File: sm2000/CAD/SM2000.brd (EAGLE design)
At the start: 160 x 100 mm, 344 parts, among them CN1 HDR100-3, CN10 ST-3509, CN11 HDR100-3, CN2 JS-MU3-002, CN3 DS-0518, CN5 ST-3509, CN8 ST-3509, J1 JMP-2PIN, J2 JMP-2PIN, J3 JMP-2PIN, J4 CONN-BOOM-XH-2A, P10 TPAD50, P11 TPAD50, P12 TPAD50, P13 TPAD50, P14 TPAD50, P16 TPAD50, P18 TPAD50, P19 TPAD50, P20 TPAD50, P21 TPAD50, P3 TPAD50, P4 TPAD50, P5 TPAD50, P6 TPAD50, P7 TPAD50, P8 TPAD50, P9 TPAD50, Q1 MMBT3904, Q12 BRF92, Q13 BFQ19, Q14 RD01MUS2, Q17 MMT2904, Q18 MMT2904, Q2 MMBT3904, Q3 MMBT3904, Q4 MMBT3904, Q5 MMBT3904, Q6 MMBT3904, Q7 BC548, Q8 BC549, SW1 SW-LC2259, SW2 TS-026, SW3 SW-LC2259EENP, SW4 TS-026, SW5 TS-02B, U1 STM32F405VGT6, U10 DNL, U12 PGA-103+, U13 ADE-1, U2 LD3985M33R, U3 STMPS2141, U4 EMIF02-USB03F2, U5 TPS54329E, U7 SA612A, U8 LM386M-1, U9 LMV341, X1 BU-SMA-H, X2 BU-SMA-H

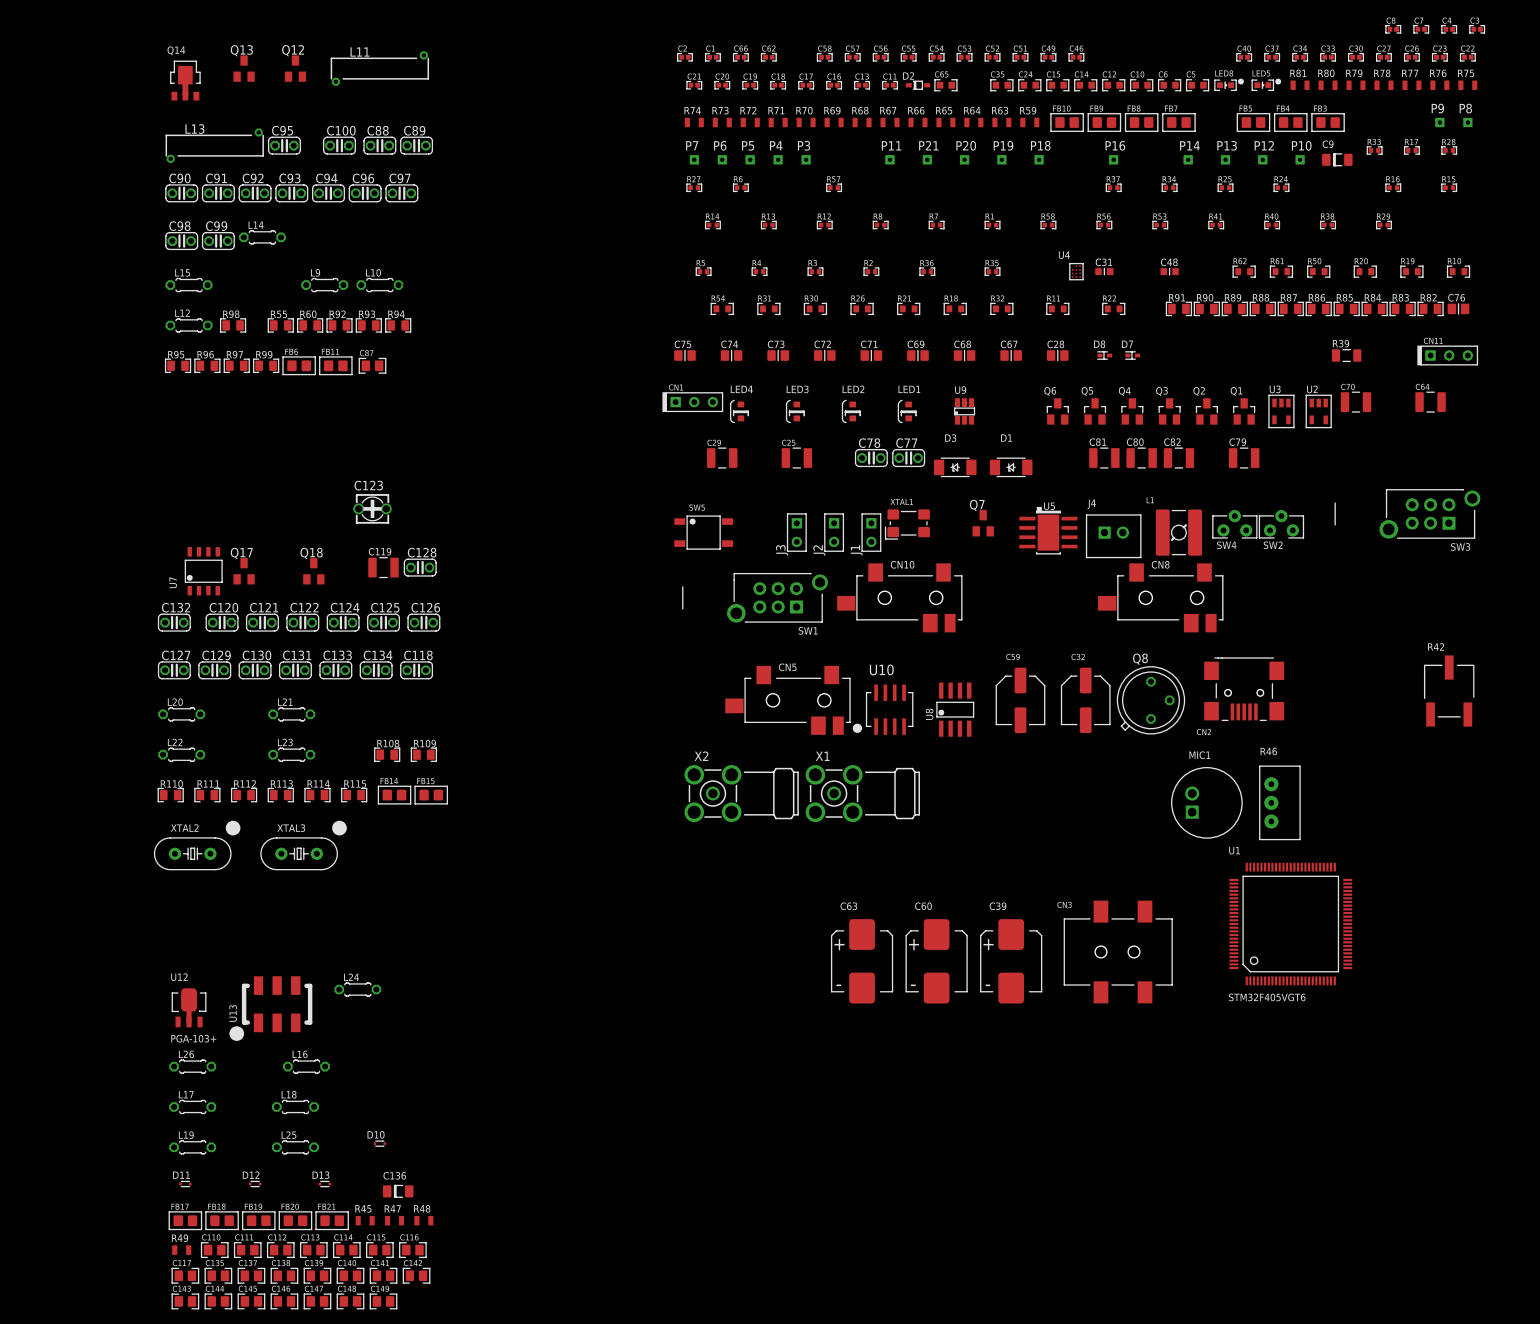
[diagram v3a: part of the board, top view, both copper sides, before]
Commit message: aDDED lOCAL oSCILLATOR CIRCUITRY TO sm2000 sch. MOVED 3.3V PS TO SHT 4. CONTINUED SCHEMATIC CLEANUP RGB
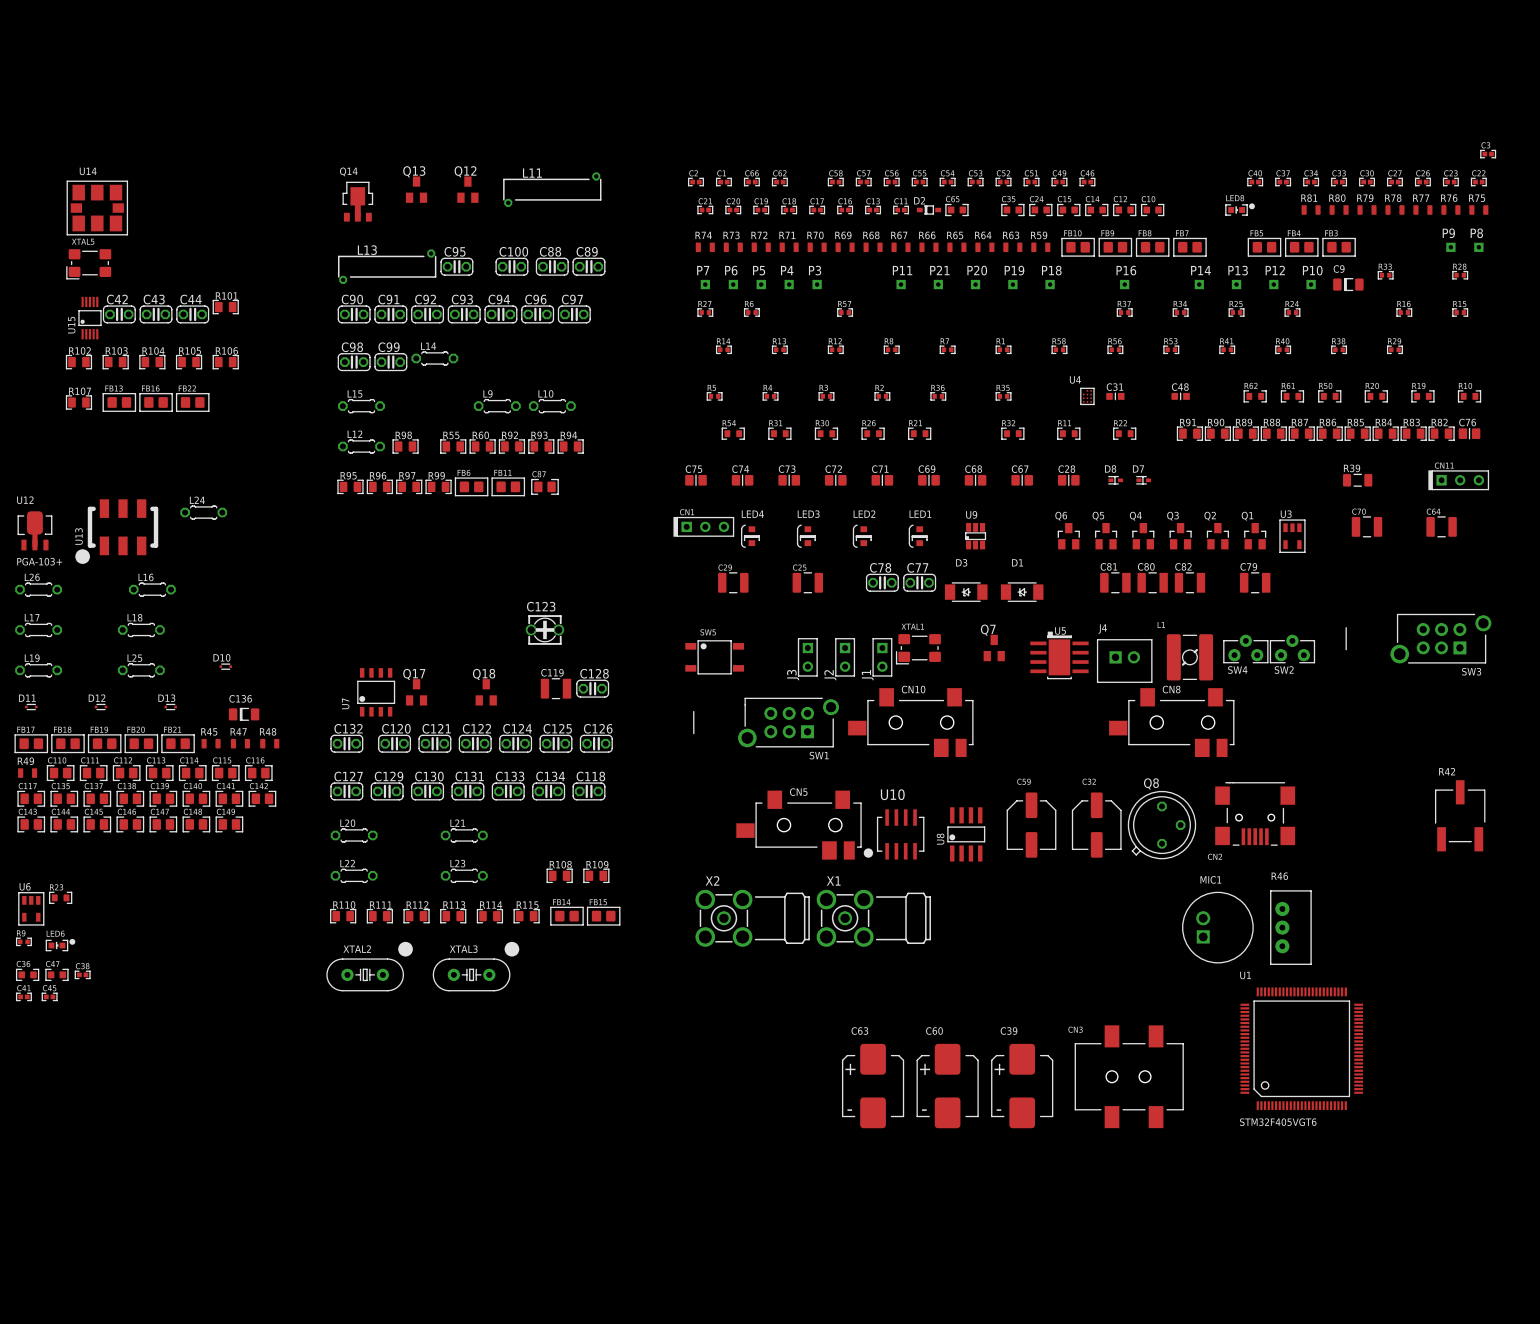
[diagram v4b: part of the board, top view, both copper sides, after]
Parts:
- removed C4, C7: 100nF,25V, AA-ipc-7351-capacitor:CAPC1005X60N
- removed C5, C6: 1uF,16V, AA-ipc-7351-capacitor:CAPC1608X92N
- removed C8: 10nF,25V, AA-ipc-7351-capacitor:CAPC1005X60N
- removed LED5: DNL, _RoweTel:SML-LX0603SRW
- removed R17: DNL, AA-ipc-7351-resistor:RESC1005X40AN
- removed R18: 0 Ohm, AA-ipc-7351-resistor:RESC1608X55N
- removed U2: LD3985M33R, _RoweTel:SOT23-5L
- added C36, C47: 1uF,16V, AA-ipc-7351-capacitor:CAPC1608X92N
- added C38: 10nF,25V, AA-ipc-7351-capacitor:CAPC1005X60N
- added C41, C45: 100nF,25V, AA-ipc-7351-capacitor:CAPC1005X60N
- added C42, C43, C44: 0.1u, rcl:C025-024X044
- added FB13, FB16, FB22: FB0805, _RoweTel:FE0805
- added LED6: DNL, _RoweTel:SML-LX0603SRW
- added R101, R104: 150, AA-ipc-7351-resistor:RESC2012X70N
- added R102, R103: 1k, AA-ipc-7351-resistor:RESC2012X70N
- added R105, R106, R107: 0R, AA-ipc-7351-resistor:RESC2012X70N
- added R23: 0 Ohm, AA-ipc-7351-resistor:RESC1608X55N
- added R9: DNL, AA-ipc-7351-resistor:RESC1005X40AN
- added U14: SI570CAC000141DG, _RoweTel:SI570
- added U15: SI5351A, _RoweTel:MSOP10
- added U6: LD3985M33R, _RoweTel:SOT23-5L
- added XTAL5: 25MHz 10pF e.g. TXC 7B-25.000MEEQ-T, _RoweTel:XTAL-FY0800035
- moved C110 68.3 mm to (-207.0, 32.0)
- moved C111 68.3 mm to (-202.5, 32.0)
- moved C112 68.3 mm to (-198.0, 32.0)
- moved C113 68.3 mm to (-193.5, 32.0)
- moved C114 68.3 mm to (-189.0, 32.0)
- moved C115 68.3 mm to (-184.5, 32.0)
- moved C116 68.3 mm to (-180.0, 32.0)
- moved C117 68.3 mm to (-211.0, 28.5)
- moved C135 68.3 mm to (-206.5, 28.5)
- moved C136 68.3 mm to (-182.0, 40.0)
- moved C137 68.3 mm to (-202.0, 28.5)
- moved C138 68.3 mm to (-197.5, 28.5)
- moved C139 68.3 mm to (-193.0, 28.5)
- moved C140 68.3 mm to (-188.5, 28.5)
- moved C141 68.3 mm to (-184.0, 28.5)
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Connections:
- removed net N$12: C8.1, U2.4
- removed net N$19: LED5.A, R17.1
- new net 1ST_LO: R105.1, R106.1, R107.1
- new net 3V3: FB13.1, FB22.1
- new net N$117: FB16.1
- new net N$119: C43.1, FB16.2, U14.2, U14.6
- new net N$120: C44.1, FB22.2, U15.7
- new net N$121: R105.2, U15.9
- new net N$122: R106.2, U15.6
- new net N$123: R107.2, U14.4
- new net N$124: R102.2, R103.2, U15.10
- new net N$37: C38.1, U6.4
- new net N$52: LED6.A, R9.1
- new net N$63: C42.1, FB13.2, U15.1
- new net N$65: U15.2, XTAL5.3
- new net N$80: U15.3, XTAL5.1
- new net RX-2ND-LO: R101.1, R103.1
- new net TX-2ND-LO: R102.1, R104.1
- net +3.3V: now also C36.1, C41.1, R23.1, R9.2, U6.5; no longer C4.1, C5.1, R17.2, R18.1, U2.5
- net +5V: now also C45.1, C47.1, U6.1, U6.3; no longer C6.1, C7.1, U2.1, U2.3
- net GND: now also C36.2, C38.2, C41.2, C42.2, C43.2, C44.2, C45.2, C47.2, LED6.C, R101.2, R104.2, U14.3, U15.8, U6.2, XTAL5.2, XTAL5.4; no longer C4.2, C5.2, C6.2, C7.2, C8.2, LED5.C, U2.2
- net VDD: now also R23.2; no longer R18.2

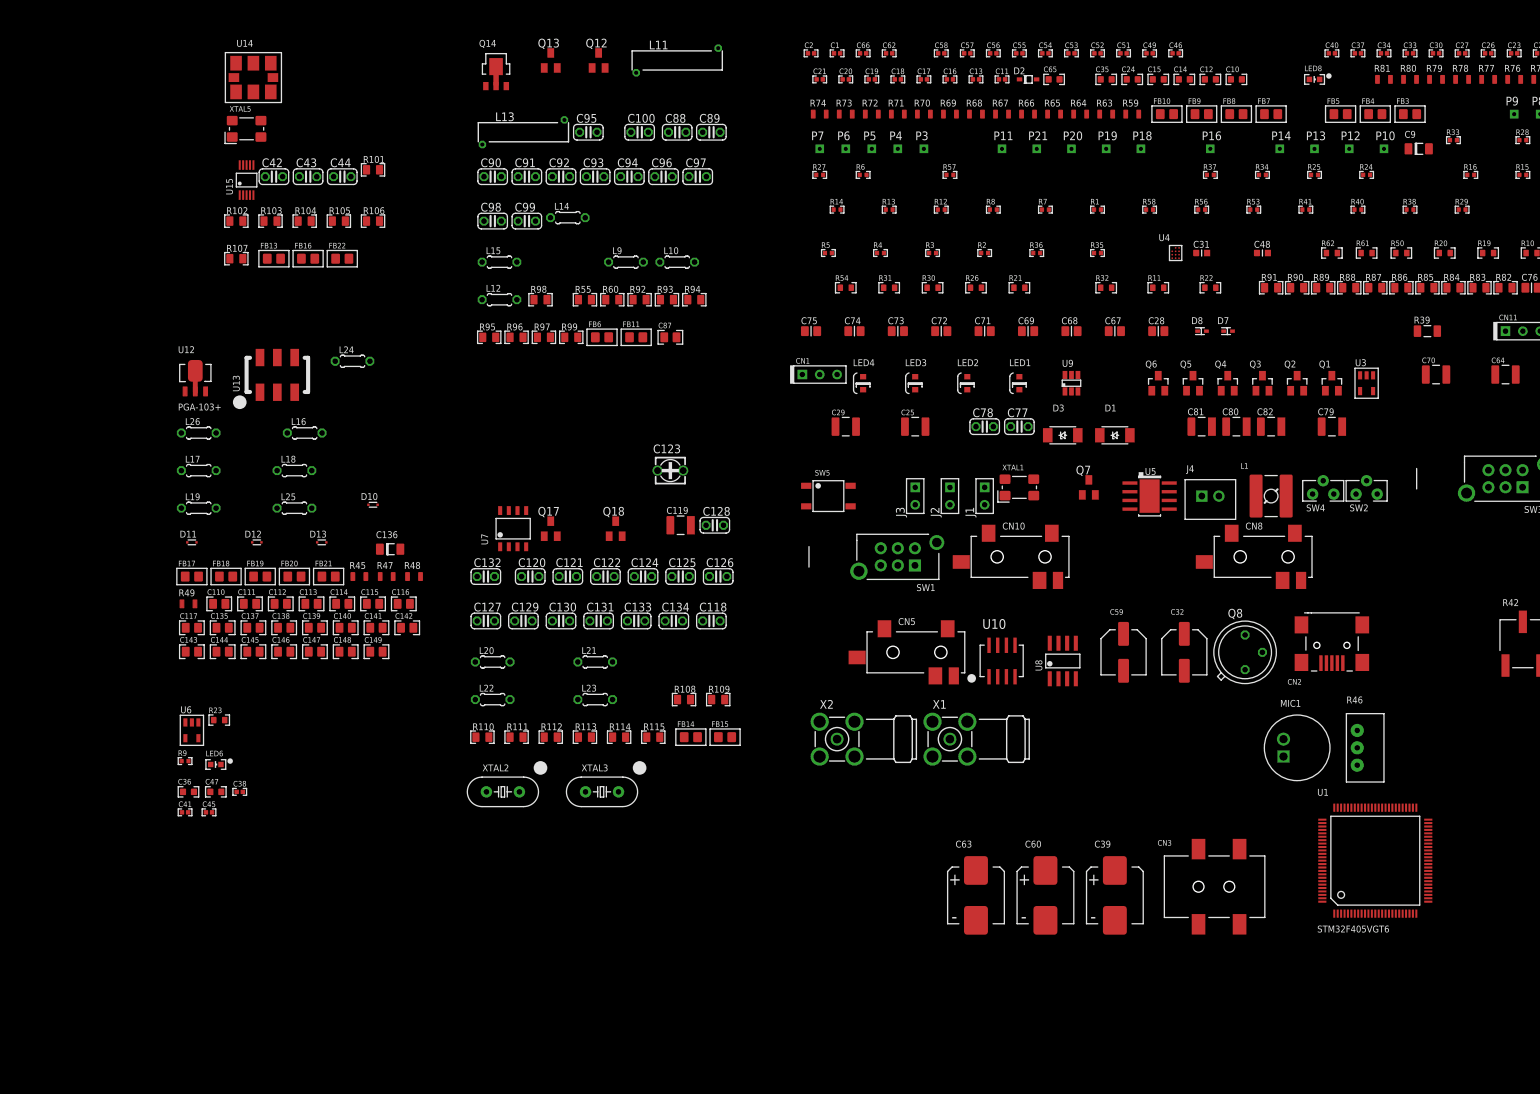
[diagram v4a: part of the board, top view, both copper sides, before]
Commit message: Intermediate Schematic Cleanup Added +9, +5 & +3.3V regulators RGB
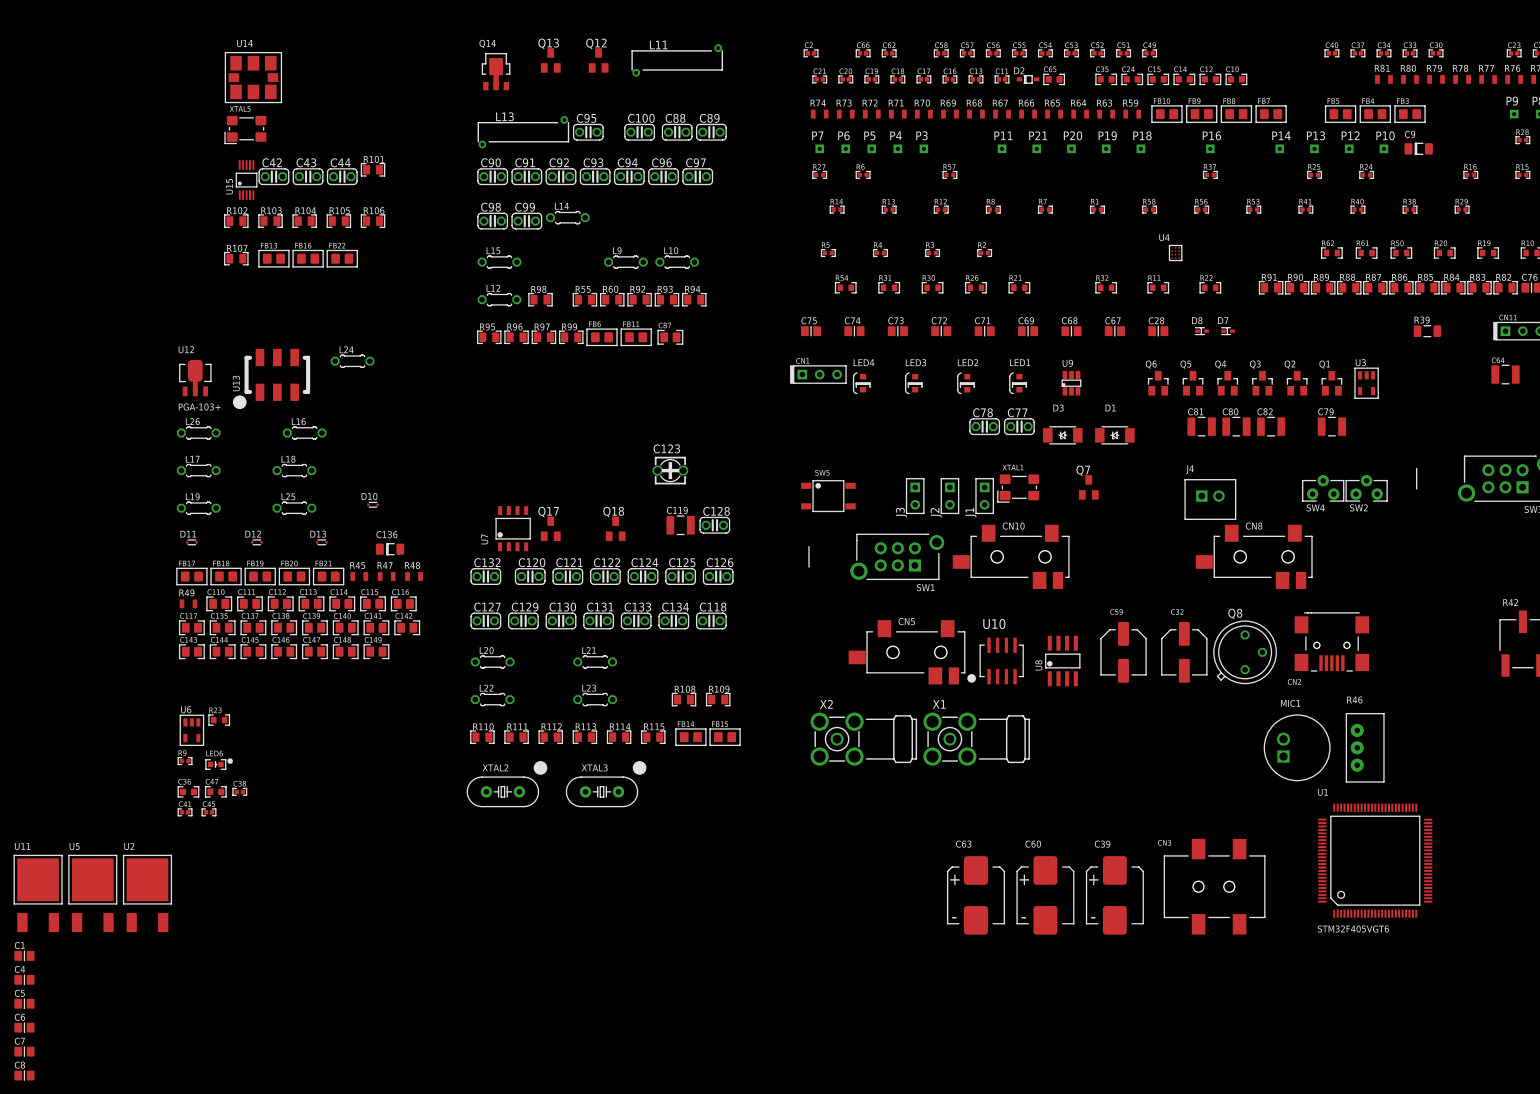
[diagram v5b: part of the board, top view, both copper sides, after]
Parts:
- removed C25, C70: 22uF,25V,1210, ipc-7351-capacitor:CAPC3225X168N
- removed C26, C46: 100nF,25V, AA-ipc-7351-capacitor:CAPC1005X60N
- removed C27: 20pF,50V, AA-ipc-7351-capacitor:CAPC1005X60N
- removed C29: 22uF,25V,1210, AA-ipc-7351-capacitor:CAPC3225X168N
- removed C31: 8.2nF,25V, ipc-7351-capacitor:CAPC1608X92N
- removed C48: 470nF,25V, ipc-7351-capacitor:CAPC1608X92N
- removed L1: 4.2uH, _RoweTel:SRR5028
- removed LED8: DNL, _RoweTel:SML-LX0603SRW
- removed R33: DNL, AA-ipc-7351-resistor:RESC1005X40AN
- removed R34: 10K,1%, AA-ipc-7351-resistor:RESC1005X40AN
- removed R35: 124.0K,1%, AA-ipc-7351-resistor:RESC1005X40AN
- removed R36: 22.1K,1%, AA-ipc-7351-resistor:RESC1005X40AN
- added C4, C6: 100nF,25V,CER, _RoweTel:C0805
- added C5, C7: .33uF,25V,CER, _RoweTel:C0805
- added C8: 100nF,25V,cer, _RoweTel:C0805
- added U11, U2: L78MXX, _RoweTel:DPAK
- C1: value 1nF,25V,0402 -> .33uF,25V,CER; device AA-ipc-7351-capacitor:CAPC1005X60N -> _RoweTel:C0805
- U5: value TPS54329E -> L78MXX; device _RoweTel:PSO-DDA -> _RoweTel:DPAK
- moved C1 177.7 mm to (-235.5, -19.5)
- moved U5 165.6 mm to (-225.5, -11.5)
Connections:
- removed net N$116: L13.1
- removed net N$138: C139.2
- removed net N$155: C147.1, R48.2
- removed net N$21: C26.1, U5.1
- removed net N$30: C27.2, R35.2, R36.1, U5.5
- removed net N$36: C1.2, C25.1, C46.1, C70.1, R21.2, R34.1, U5.2
- removed net N$38: C31.1, U5.8
- removed net N$40: C48.1, U5.6
- removed net N$42: R34.2, U5.7
- removed net N$47: LED8.A, R33.2
- removed net N$50: U7.2
- removed net SW: C26.2, L1.1, U5.3
- new net +9V: C4.1, L13.1, U2.3
- new net ANT_SMA: C100.1, C147.1, L14.2, R48.2
- new net N$54: C1.1, C5.1, C7.1, R21.2, U11.1, U2.1, U5.1
- net +5V: now also C6.1, U5.3; no longer C27.1, C29.1, L1.2, R33.1, R35.1
- net GND: now also C1.2, C4.2, C5.2, C6.2, C7.2, C8.2, U11.4, U2.4; no longer C1.1, C25.2, C29.2, C31.2, C46.2, C48.2, C70.2, LED8.C, R36.2, U5.EP
- net N$11: now also C139.2, U12.1; no longer C100.1, L14.2
- net N$51: now also U7.2
- net VDD: now also C8.1, U11.3
